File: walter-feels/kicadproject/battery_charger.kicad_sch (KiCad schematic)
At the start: 62 parts, among them IC1 LTC4015EUHF#PBF, Q1 FDMC8030, Q2 FDMC8327L, Q3 SI7611DN-T1-GE3

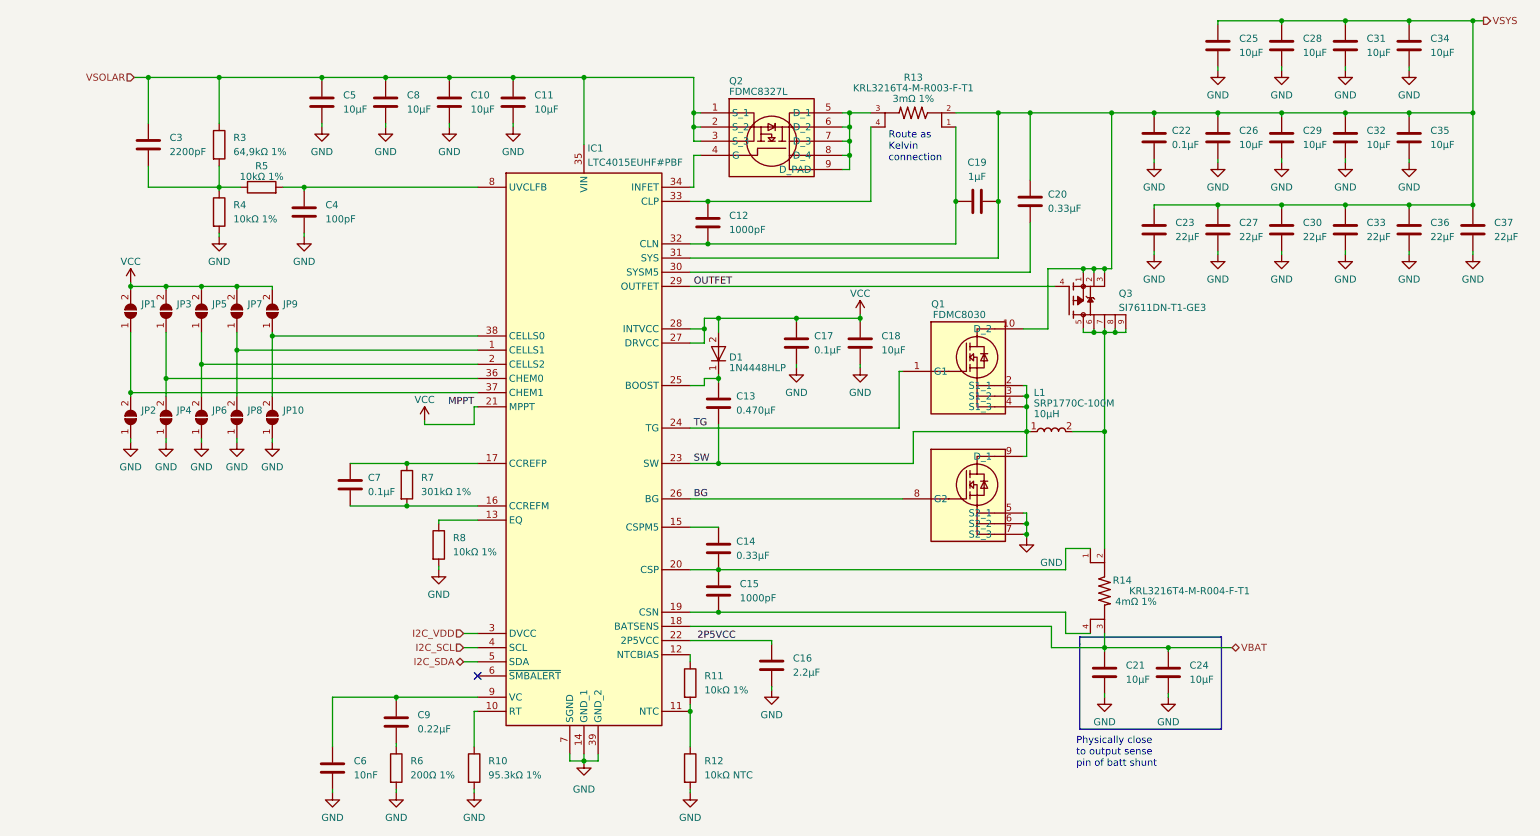
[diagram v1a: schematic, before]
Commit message: Updated Walter Feels to V2.3
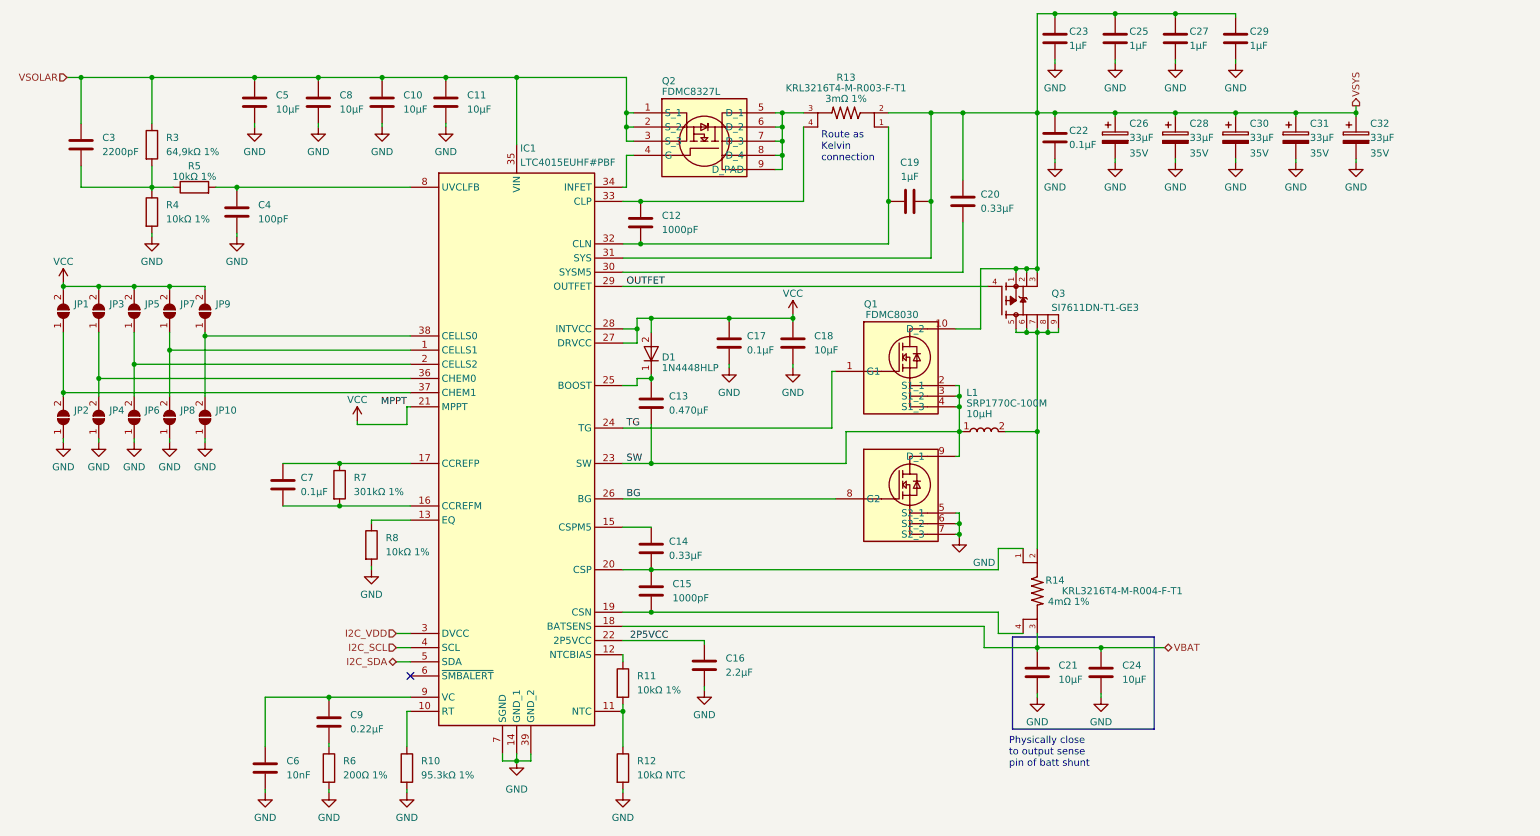
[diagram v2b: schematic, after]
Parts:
- removed C26, C28, C31, C32, C34, C35: 10µF, Capacitor_SMD:C_1206_3216Metric, symbol Device:C
- removed C30, C33, C36, C37: 22µF, Capacitor_SMD:C_1206_3216Metric, symbol Device:C
- added C26, C28, C30, C31, C32: 33µF, Capacitor_Tantalum_SMD:CP_EIA-7343-30_AVX-N, symbol Device:C_Polarized
- C23, C27: value 22µF -> 1μF; footprint Capacitor_SMD:C_1206_3216Metric -> Capacitor_SMD:C_0603_1608Metric; JLCPCB C12891 -> C15849
- C25, C29: value 10µF -> 1μF; footprint Capacitor_SMD:C_1206_3216Metric -> Capacitor_SMD:C_0603_1608Metric; JLCPCB C13585 -> C15849
- JP1, JP10, JP2, JP3, JP4, JP5, JP6, JP7, JP8, JP9: now left out of the parts list
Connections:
- net GND: now also C23.1, C25.1, C27.1, C29.1, C26.2, C28.2, C30.2, C31.2, C32.2; no longer C23.2, C25.2, C27.2, C29.2
- net VSYS: now also C23.2, C25.2, C27.2, C29.2, C26.1, C28.1, C30.1, C31.1, C32.1; no longer C23.1, C25.1, C27.1, C29.1
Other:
- moved on the sheet: C10, C11, C12, C13, C14, C15, C16, C17, C18, C19, C20, C21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

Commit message: Updated Walter Feels project to version 2.6
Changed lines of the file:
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@@
   (title_block
     (title "Walter Feels")
-    (date "2025-02-12")
-    (rev "2.4")
+    (date "2026-01-13")
+    (rev "2.6")
     (company "DPTechnics BV")
     (comment 1 "Checked by: Jonas Maes")
@@
     (stroke (width 0) (type default) (color 0 0 0 0))
   )
+  (wire (pts (xy 24.13 36.195) (xy 24.13 37.465))
+    (stroke (width 0) (type default) (color 0 0 0 0))
+  )
   (wire (pts (xy 181.61 119.38) (xy 181.61 120.015))
     (stroke (width 0) (type default) (color 0 0 0 0))
@@
   (label "SW" (at 121.92 106.68 0)
     (effects (font (size 1.27 1.27)) (justify left bottom))
-  )
-  (label "MPPT" (at 82.55 96.52 180)
-    (effects (font (size 1.27 1.27)) (justify right bottom))
   )
   (label "2P5VCC" (at 122.555 138.43 0)
@@
     (pin "2")
   )
+  (symbol (lib_id "power:PWR_FLAG") (at 24.13 36.195 0) (unit 1)
+    (in_bom yes) (on_board yes)
+    (property "Reference" "#FLG0102" (id 0) (at 24.13 34.29 0)
+      (effects (font (size 1.27 1.27)) hide)
+    )
+    (property "Value" "PWR_FLAG" (id 1) (at 24.13 32.385 0))
+    (property "Footprint" "" (id 2) (at 24.13 36.195 0)
+      (effects (font (size 1.27 1.27)) hide)
+    )
+    (property "Datasheet" "~" (id 3) (at 24.13 36.195 0)
+      (effects (font (size 1.27 1.27)) hide)
+    )
+    (pin "1")
+  )
   (symbol (lib_id "Device:C") (at 151.765 85.09 0) (unit 1)
